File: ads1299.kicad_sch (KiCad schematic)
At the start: 35 parts, among them IC3 ADS1299-4PAGR, J4 Conn_01x06

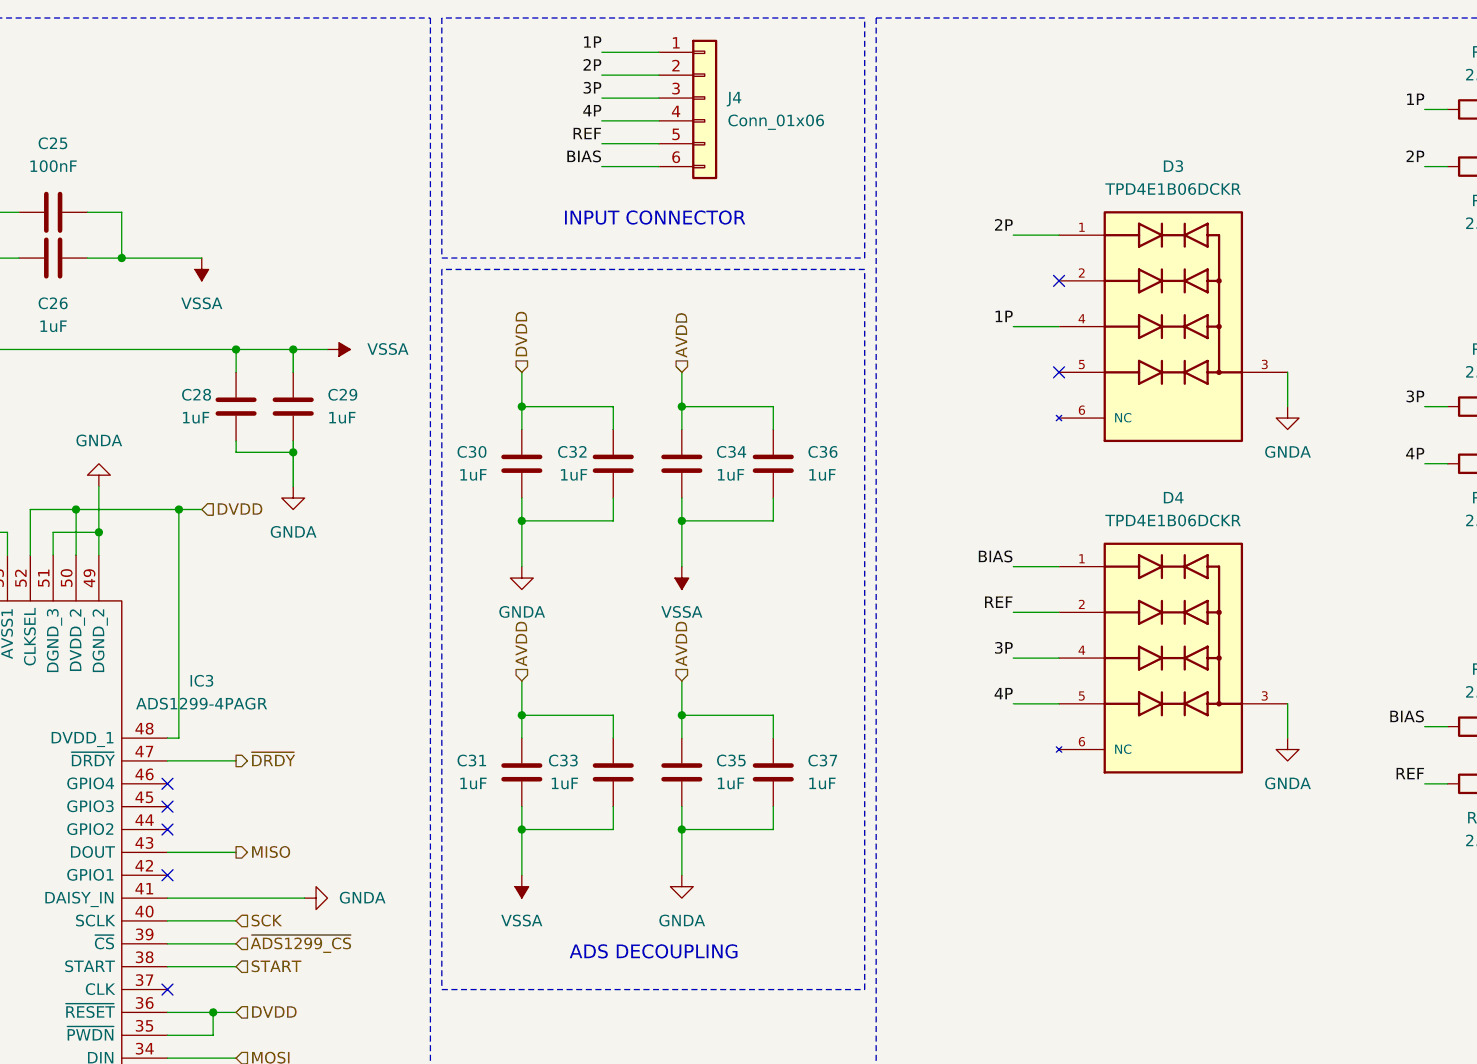
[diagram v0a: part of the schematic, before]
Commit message: Feat: 개발보드 버전으로 PCB 변경
수정사항

단가 감소
- PCB Board size up (50x50)
- blind via 제거 (전체 레이아웃 수정)
- AVDD 전력평면 추가
- ADS1299 안쓰는핀 GND
- ADS1299 배치 변경 (Layout Reference 적용)

개발보드만 적용사항
- Pin Header size up 1.27 → 2.54mm
- PCB Size 50x50(mm)
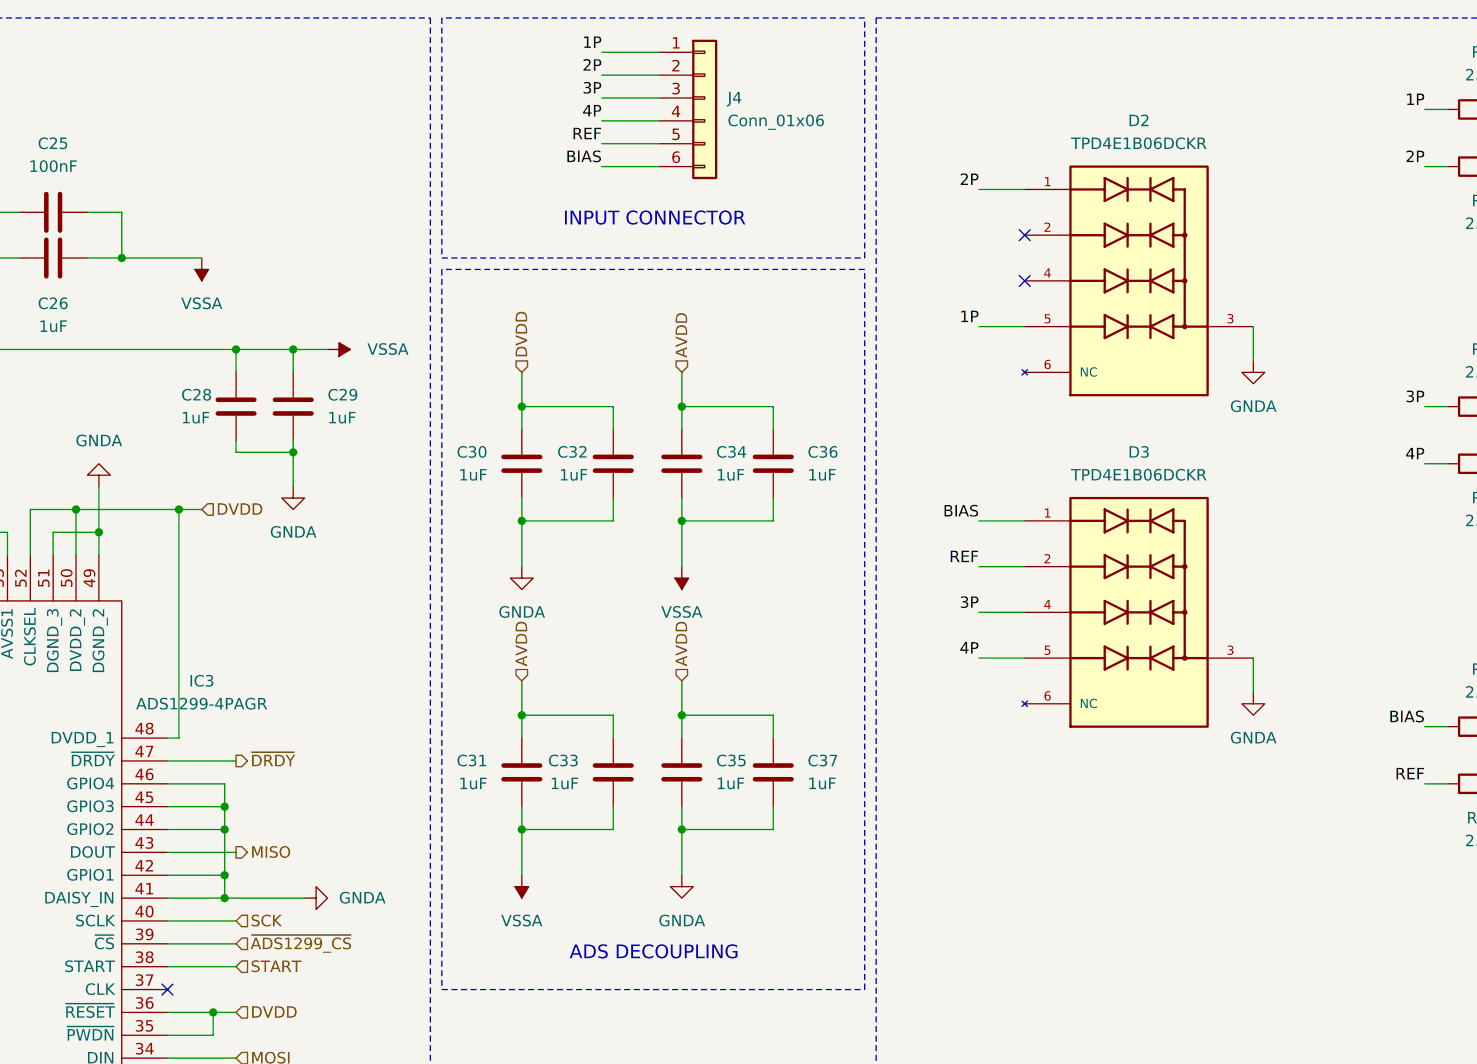
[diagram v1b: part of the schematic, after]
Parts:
- removed D4: TPD4E1B06DCKR, TPD4E1B06DCKR:TVS_TPD4E1B06DCKR, symbol TPD4E1B06DCKR:TPD4E1B06DCKR
- added D2: TPD4E1B06DCKR, TPD4E1B06DCKR:TVS_TPD4E1B06DCKR, symbol TPD4E1B06DCKR:TPD4E1B06DCKR
- C24: footprint Capacitor_SMD:C_0402_1005Metric -> Capacitor_SMD:C_0805_2012Metric
- J4: footprint Connector_PinHeader_1.27mm:PinHeader_1x06_P1.27mm_Vertical -> Connector_PinHeader_2.54mm:PinHeader_1x06_P2.54mm_Vertical
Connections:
- net 1P: now also D2.5; no longer D3.4
- net 2P: now also D2.1; no longer D3.1
- net 3P: now also D3.4
- net 4P: now also D3.5
- net BIAS: now also D3.1
- net GNDA: now also IC3.42 (GPIO1), IC3.44 (GPIO2), IC3.45 (GPIO3), IC3.46 (GPIO4), D2.3
- net REF: now also D3.2
- no-connect marks 20 -> 16

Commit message: Doc: Gerber Data V0.2(dev)
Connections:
- net GNDA: no longer IC3.42 (GPIO1), IC3.44 (GPIO2), IC3.45 (GPIO3), IC3.46 (GPIO4)
- no-connect marks 16 -> 20
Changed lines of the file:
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@@
-	)
-	(junction
-		(at 97.79 110.49)
-		(diameter 0)
-		(color 0 0 0 0)
 	)
 	(junction
@@
 	)
 	(junction
-		(at 97.79 102.87)
-		(diameter 0)
-		(color 0 0 0 0)
-	)
-	(junction
 		(at 63.5 69.85)
 		(diameter 0)
@@
 	)
 	(junction
-		(at 97.79 107.95)
-		(diameter 0)
-		(color 0 0 0 0)
-	)
-	(junction
 		(at 148.59 102.87)
 		(diameter 0)
@@
 	(junction
 		(at 99.06 49.53)
-		(diameter 0)
-		(color 0 0 0 0)
-	)
-	(junction
-		(at 97.79 100.33)
 		(diameter 0)
 		(color 0 0 0 0)
@@
 	)
 	(no_connect
+		(at 91.44 100.33)
+	)
+	(no_connect
 		(at 38.1 100.33)
+	)
+	(no_connect
+		(at 91.44 107.95)
 	)
 	(no_connect
@@
 	)
 	(no_connect
+		(at 91.44 97.79)
+	)
+	(no_connect
 		(at 38.1 92.71)
 	)
@@
 		(at 38.1 110.49)
 	)
+	(no_connect
+		(at 91.44 102.87)
+	)
 	(wire
 		(pts
@@
 	(wire
 		(pts
-			(xy 91.44 102.87) (xy 97.79 102.87)
-		)
-		(stroke
-			(width 0)
-			(type default)
-		)
-	)
-	(wire
-		(pts
 			(xy 130.81 58.42) (xy 130.81 55.88)
 		)
@@
 	(wire
 		(pts
-			(xy 91.44 107.95) (xy 97.79 107.95)
-		)
-		(stroke
-			(width 0)
-			(type default)
-		)
-	)
-	(wire
-		(pts
 			(xy 83.82 64.77) (xy 83.82 69.85)
 		)
@@
 		)
 	)
-	(wire
-		(pts
-			(xy 97.79 102.87) (xy 97.79 107.95)
-		)
-		(stroke
-			(width 0)
-			(type default)
-		)
-	)
 	(polyline
 		(pts
@@
 	(wire
 		(pts
-			(xy 97.79 97.79) (xy 97.79 100.33)
-		)
-		(stroke
-			(width 0)
-			(type default)
-		)
-	)
-	(wire
-		(pts
 			(xy 130.81 55.88) (xy 140.97 55.88)
 		)
@@
 	(wire
 		(pts
-			(xy 97.79 107.95) (xy 97.79 110.49)
-		)
-		(stroke
-			(width 0)
-			(type default)
-		)
-	)
-	(wire
-		(pts
 			(xy 260.35 74.93) (xy 260.35 78.74)
 		)
@@
 	(wire
 		(pts
-			(xy 91.44 110.49) (xy 97.79 110.49)
+			(xy 91.44 110.49) (xy 106.68 110.49)
 		)
 		(stroke
@@
 	(wire
 		(pts
-			(xy 91.44 97.79) (xy 97.79 97.79)
-		)
-		(stroke
-			(width 0)
-			(type default)
-		)
-	)
-	(wire
-		(pts
 			(xy 130.81 66.04) (xy 130.81 68.58)
 		)
@@
 		)
 	)
-	(wire
-		(pts
-			(xy 91.44 100.33) (xy 97.79 100.33)
-		)
-		(stroke
-			(width 0)
-			(type default)
-		)
-	)
 	(polyline
 		(pts
@@
 	(wire
 		(pts
-			(xy 97.79 110.49) (xy 106.68 110.49)
-		)
-		(stroke
-			(width 0)
-			(type default)
-		)
-	)
-	(wire
-		(pts
 			(xy 30.48 55.88) (xy 33.02 55.88)
 		)
@@
 		)
 		(stroke
-			(width 0)
-			(type default)
-		)
-	)
-	(wire
-		(pts
-			(xy 97.79 100.33) (xy 97.79 102.87)
-		)
-		(stroke
